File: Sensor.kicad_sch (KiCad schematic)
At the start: 28 parts, among them J27 *, SW2 *, U7 *, U8 *, U9 LSM6DSV

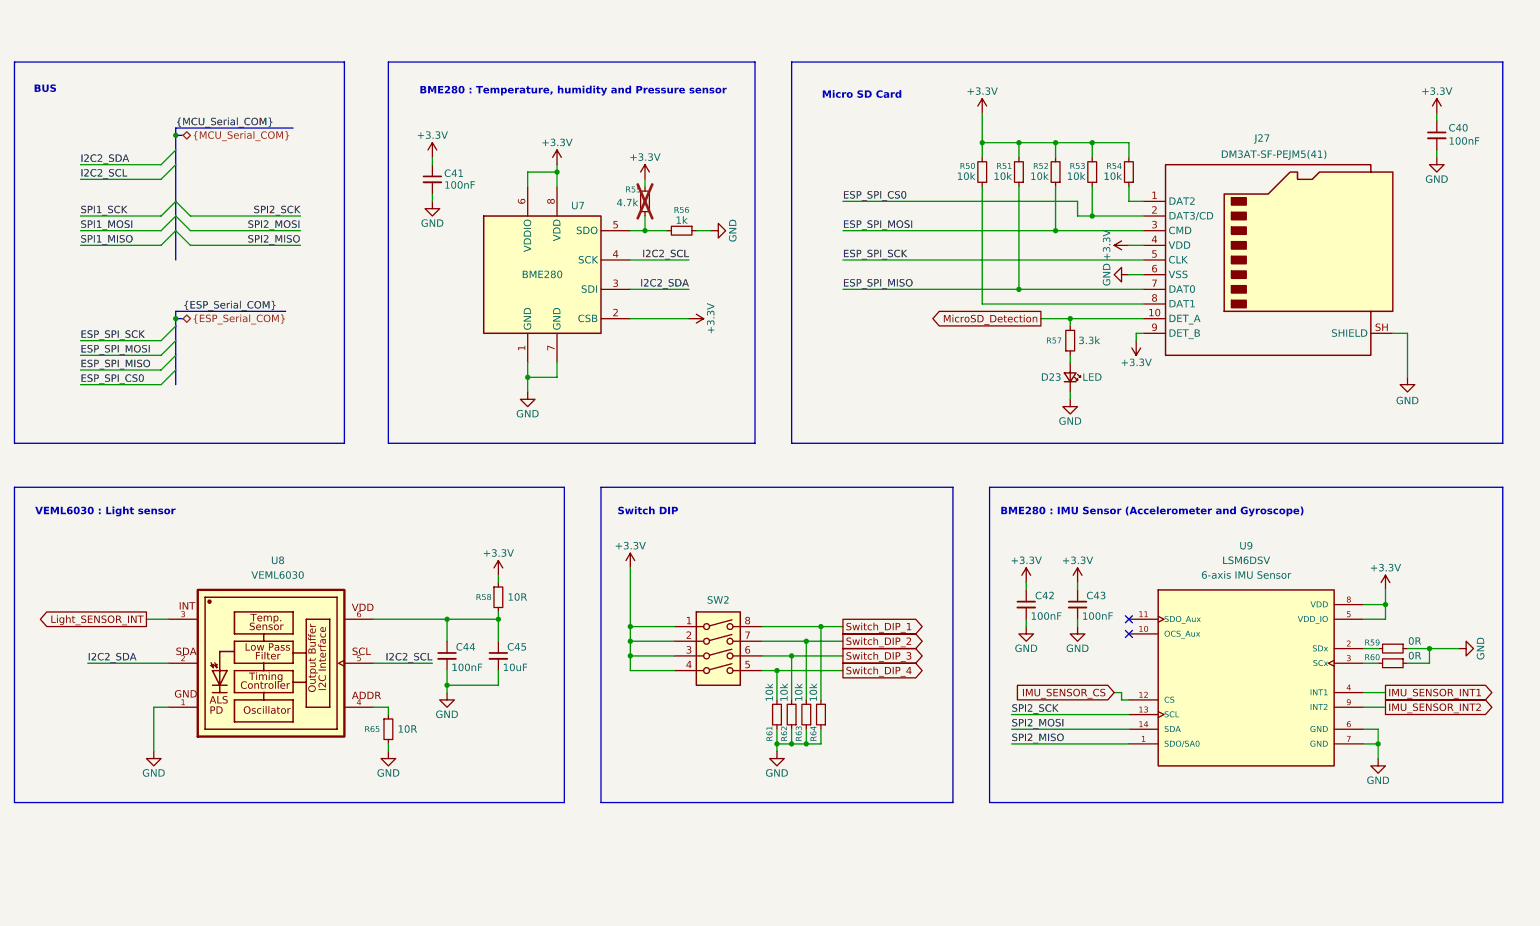
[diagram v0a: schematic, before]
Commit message: [Project][Added] CI/CD environment
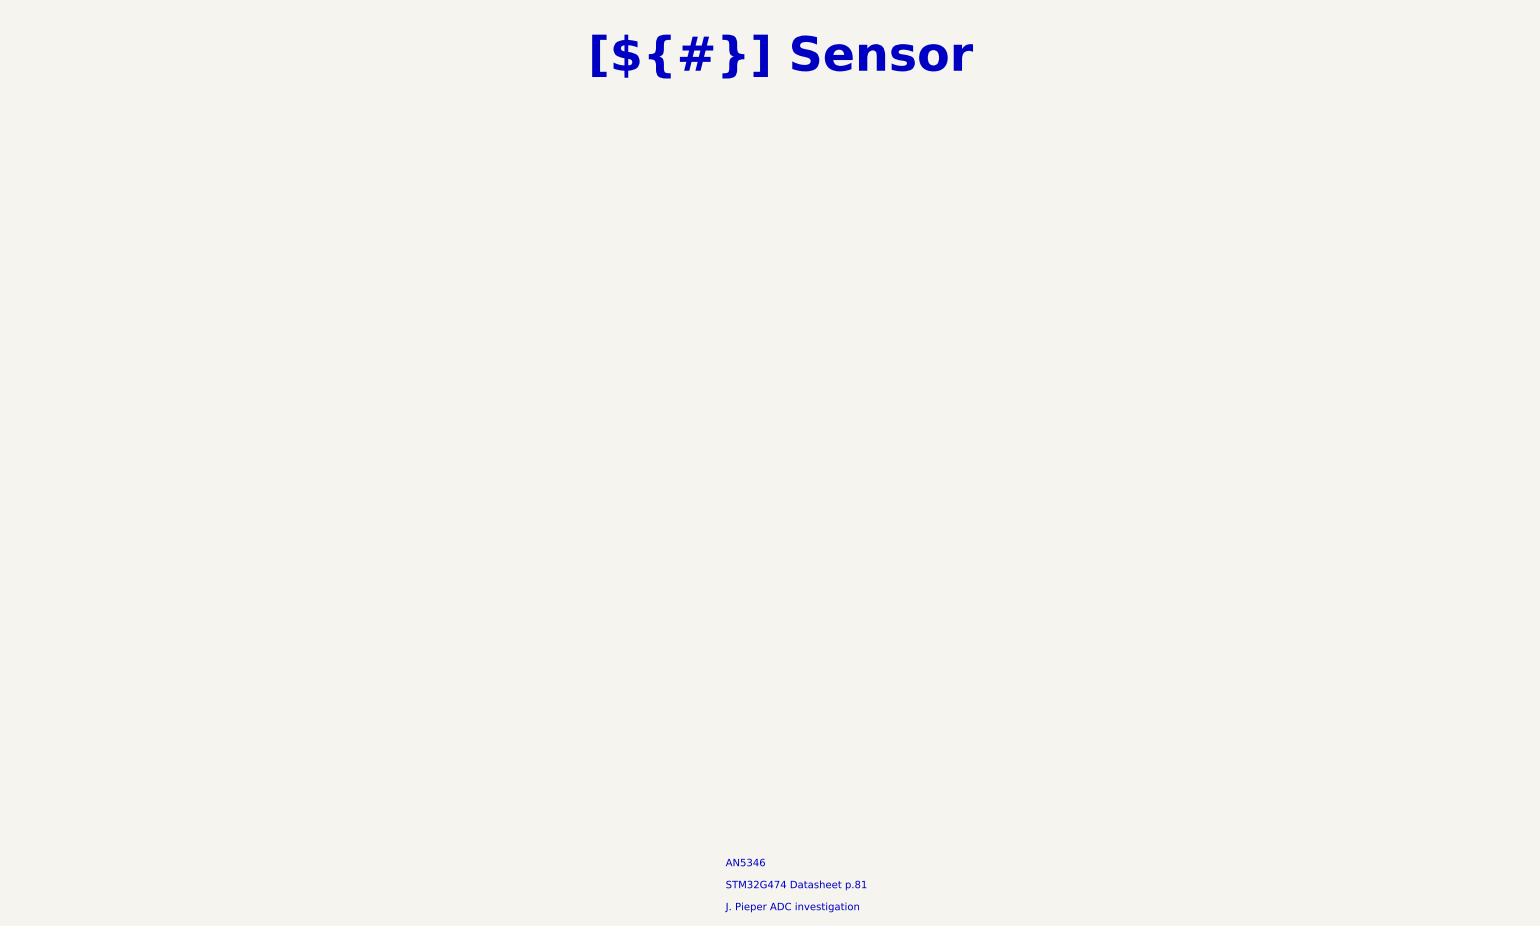
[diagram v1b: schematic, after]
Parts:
- removed C40, C41, C42, C43, C44: 100nF, Capacitor_SMD:C_0603_1608Metric_Pad1.08x0.95mm_HandSolder, symbol Device:C_Small
- removed C45: 10uF, Capacitor_SMD:C_0603_1608Metric_Pad1.08x0.95mm_HandSolder, symbol Device:C_Small
- removed D23: 5V, LED_SMD:LED_0805_2012Metric_Pad1.15x1.40mm_HandSolder, symbol Device:LED_Small
- removed J27: *, Connector_Card:microSD_HC_Hirose_DM3AT-SF-PEJM5, symbol Connector:Micro_SD_Card_Det2
- removed R50, R51, R52, R53, R54, R61, R62, R63, R64: 10k, Resistor_SMD:R_0603_1608Metric_Pad0.98x0.95mm_HandSolder, symbol Device:R_Small
- removed R55: 4.7k, Resistor_SMD:R_0603_1608Metric_Pad0.98x0.95mm_HandSolder, symbol Device:R_Small
- removed R56: 1k, Resistor_SMD:R_0603_1608Metric_Pad0.98x0.95mm_HandSolder, symbol Device:R_Small
- removed R57: 3.3k, Resistor_SMD:R_0603_1608Metric_Pad0.98x0.95mm_HandSolder, symbol Device:R_Small
- removed R58, R65: 10R, Resistor_SMD:R_0603_1608Metric_Pad0.98x0.95mm_HandSolder, symbol Device:R_Small
- removed R59, R60: 0R, Resistor_SMD:R_0603_1608Metric_Pad0.98x0.95mm_HandSolder, symbol Device:R_Small
- removed SW2: *, Button_Switch_SMD:SW_DIP_SPSTx04_Slide_Copal_CHS-04B_W7.62mm_P1.27mm, symbol Switch:SW_DIP_x04
- removed U7: *, Package_LGA:Bosch_LGA-8_2.5x2.5mm_P0.65mm_ClockwisePinNumbering, symbol Sensor:BME280
- removed U8: *, P_Specific_Footprint:VISHAY_VEML6030_2X2X0.87, symbol P_Sensor:VEML6030
- removed U9: LSM6DSV, P_LGA:LGA-14_3X2.5_P0.83mm, symbol P_Sensor:LSM6DSV
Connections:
- no-connect marks 2 -> 0
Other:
- note added: "AN5346"
- note added: "J. Pieper ADC investigation"
- note added: "STM32G474 Datasheet p.81"
- note removed: "BME280 : IMU Sensor (Accelerometer and Gyroscope)"
- note removed: "BME280 : Temperature, humidity and Pressure sensor"
- note removed: "BUS"
- note removed: "Micro SD Card"
- note removed: "Switch DIP"
- note removed: "VEML6030 : Light sensor"
- company: Nexvantis -> ${COMPANY}
- title: Data Acquisition Board -> Sensor

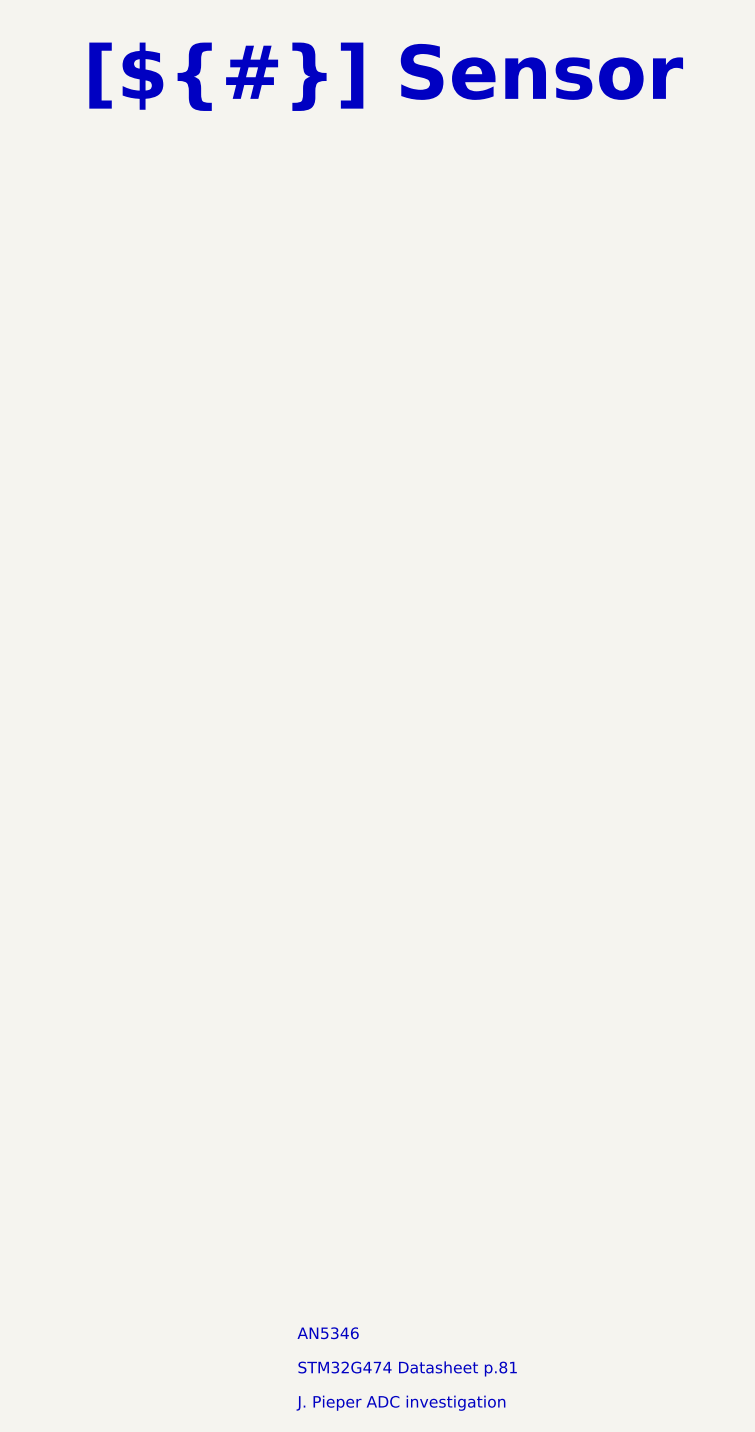
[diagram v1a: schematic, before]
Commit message: [Project][Added] CI/CD environment
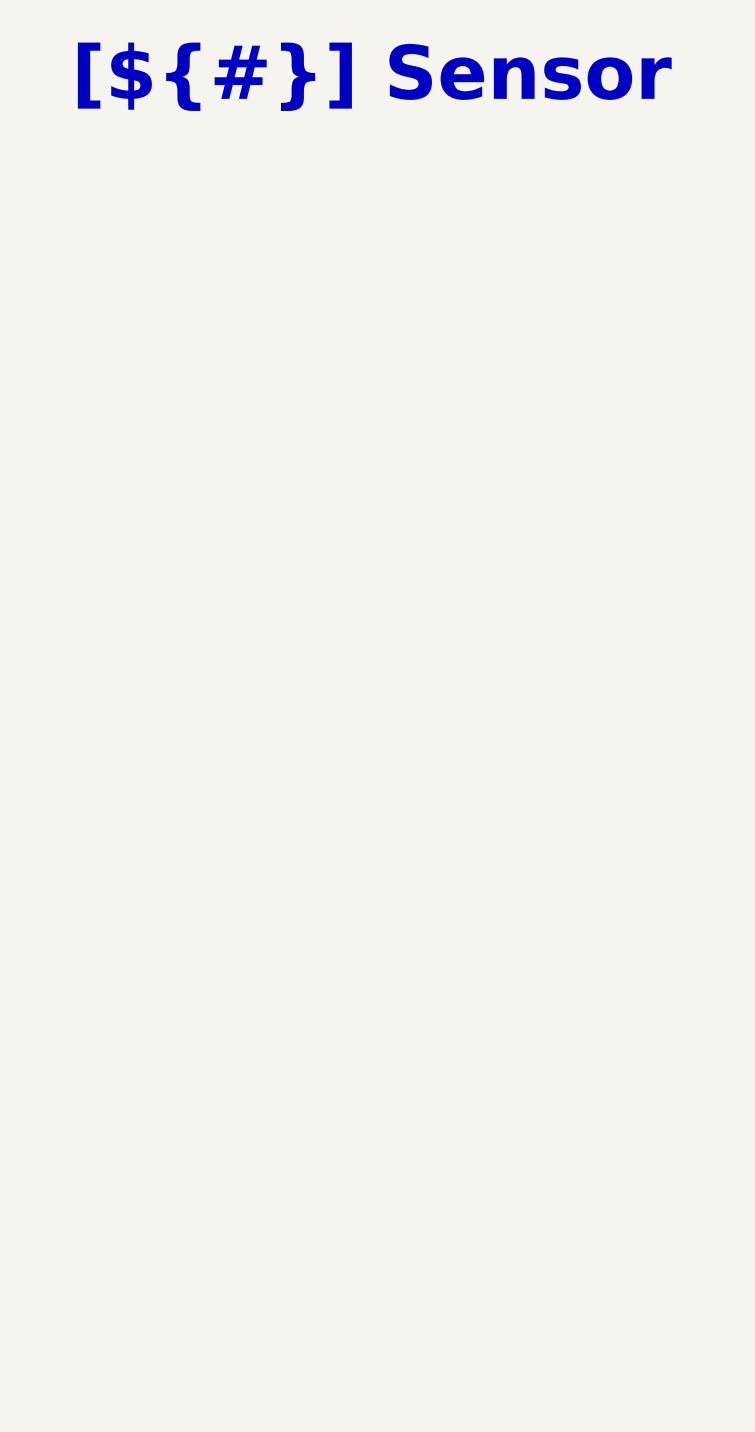
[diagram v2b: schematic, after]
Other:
- note removed: "AN5346"
- note removed: "J. Pieper ADC investigation"
- note removed: "STM32G474 Datasheet p.81"
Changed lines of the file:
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@@
 (kicad_sch
-	(version 20260306)
+	(version 20250114)
 	(generator "eeschema")
-	(generator_version "10.0")
+	(generator_version "9.0")
 	(paper "A4")
 	(title_block
@@
 		(company "${COMPANY}")
 	)
-	(text "J. Pieper ADC investigation"
-		(exclude_from_sim no)
-		(at 142.24 170.18 0)
-		(effects
-			(font
-				(face "Arial")
-				(size 1.27 1.27)
-				(color 0 0 0 1)
-			)
-			(justify left bottom)
-			(href "https://jpieper.com/2023/07/24/stm32g4-adc-performance-part-2/")
-		)
-	)
-	(text "STM32G474 Datasheet p.81"
-		(exclude_from_sim no)
-		(at 142.24 166.37 0)
-		(effects
-			(font
-				(face "Arial")
-				(size 1.27 1.27)
-				(color 0 0 0 1)
-			)
-			(justify left bottom)
-			(href "https://www.st.com/resource/en/datasheet/stm32g474cb.pdf")
-		)
-	)
-	(text "AN5346"
-		(exclude_from_sim no)
-		(at 142.24 162.56 0)
-		(effects
-			(font
-				(face "Arial")
-				(size 1.27 1.27)
-				(color 0 0 0 1)
-			)
-			(justify left bottom)
-			(href "https://www.st.com/resource/en/application_note/an5346-stm32g4-adc-use-tips-and-recommendations-stmicroelectronics.pdf")
-		)
-	)
 	(text_box "[${#}] ${TITLE}"
 		(exclude_from_sim no)
-		(at 115.57 15.24 0)
+		(at 114.3 15.24 0)
 		(size 72.39 12.7)
 		(margins 4.4999 4.4999 4.4999 4.4999)

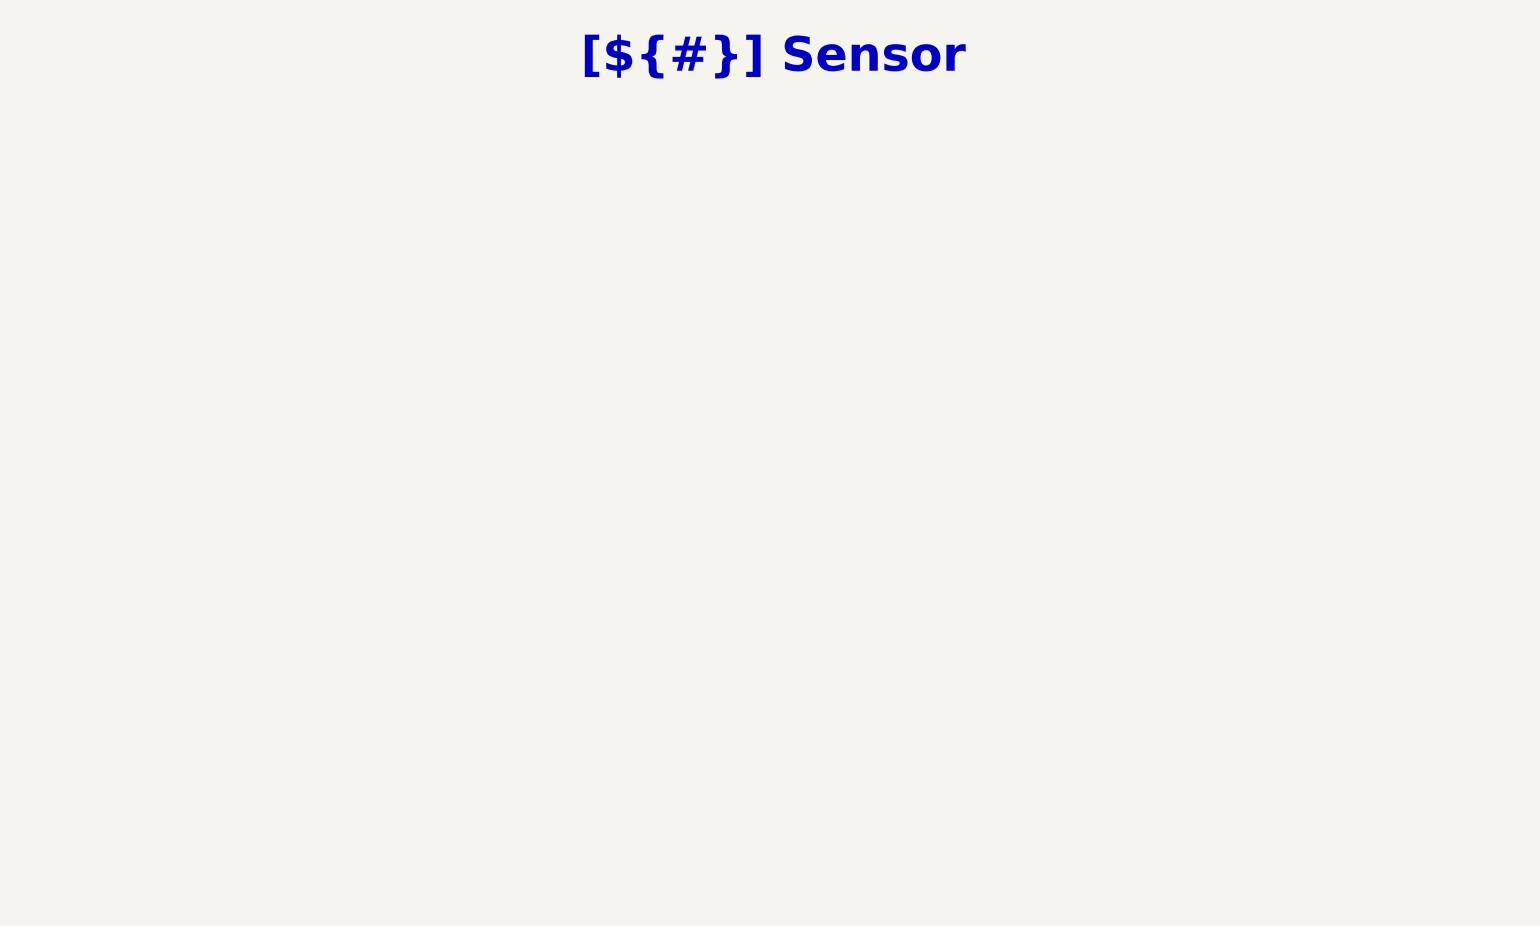
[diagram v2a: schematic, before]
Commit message: [Schematic][Add] Sensor, add schematic
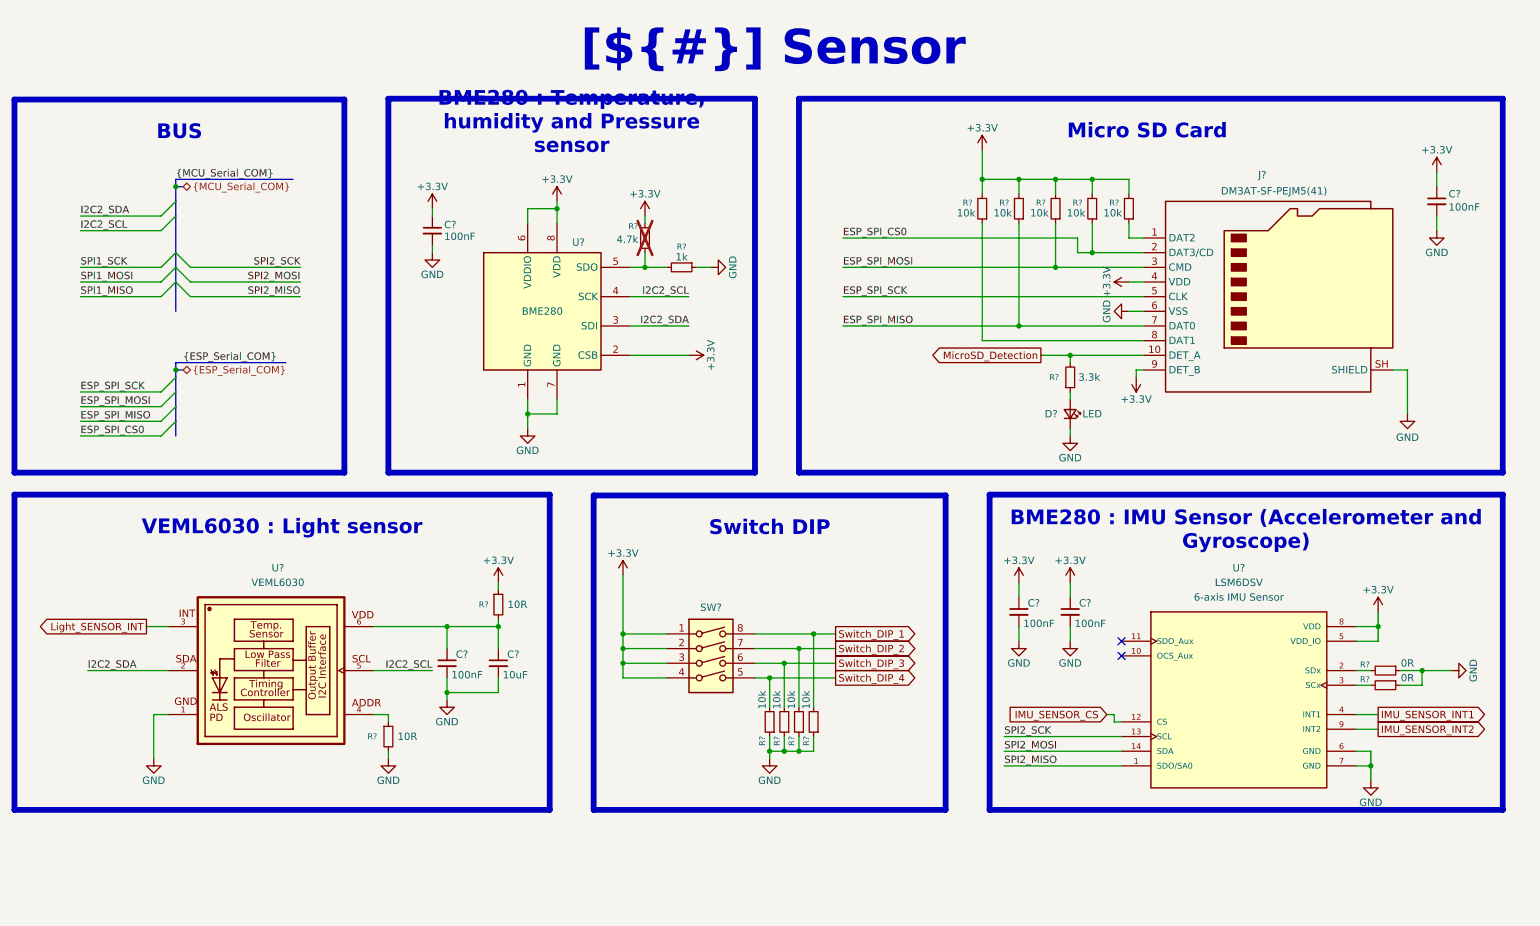
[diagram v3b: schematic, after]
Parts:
- added C? (x5): 100nF, Capacitor_SMD:C_0603_1608Metric_Pad1.08x0.95mm_HandSolder, symbol Device:C_Small
- added C?: 10uF, Capacitor_SMD:C_0603_1608Metric_Pad1.08x0.95mm_HandSolder, symbol Device:C_Small
- added D?: 5V, LED_SMD:LED_0805_2012Metric_Pad1.15x1.40mm_HandSolder, symbol Device:LED_Small
- added J?: *, Connector_Card:microSD_HC_Hirose_DM3AT-SF-PEJM5, symbol Connector:Micro_SD_Card_Det2
- added R? (x9): 10k, Resistor_SMD:R_0603_1608Metric_Pad0.98x0.95mm_HandSolder, symbol Device:R_Small
- added R?: 3.3k, Resistor_SMD:R_0603_1608Metric_Pad0.98x0.95mm_HandSolder, symbol Device:R_Small
- added R? (x2): 10R, Resistor_SMD:R_0603_1608Metric_Pad0.98x0.95mm_HandSolder, symbol Device:R_Small
- added R?: 1k, Resistor_SMD:R_0603_1608Metric_Pad0.98x0.95mm_HandSolder, symbol Device:R_Small
- added R? (x2): 0R, Resistor_SMD:R_0603_1608Metric_Pad0.98x0.95mm_HandSolder, symbol Device:R_Small
- added R?: 4.7k, Resistor_SMD:R_0603_1608Metric_Pad0.98x0.95mm_HandSolder, symbol Device:R_Small
- added SW?: *, Button_Switch_SMD:SW_DIP_SPSTx04_Slide_Copal_CHS-04B_W7.62mm_P1.27mm, symbol Switch:SW_DIP_x04
- added U?: *, Package_LGA:Bosch_LGA-8_2.5x2.5mm_P0.65mm_ClockwisePinNumbering, symbol Sensor:BME280
- added U?: *, P_Specific_Footprint:VISHAY_VEML6030_2X2X0.87, symbol P_Sensor:VEML6030
- added U?: LSM6DSV, P_LGA:LGA-14_3X2.5_P0.83mm, symbol P_Sensor:LSM6DSV
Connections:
- new net: C?.1, C?.1, R?.2, U?.6
- new net: D?.2 (A), R?.1
- new net: J?.1 (DAT2), R?.1
- new net: J?.8 (DAT1), R?.1
- new net: R?.1, U?.4
- new net: R?.1, R?.2, U?.5 (SDO)
- new net: R?.2, U?.2 (SDx)
- new net: R?.2, U?.3 (SCx)
- new net +3.3V: C?.1, C?.1, C?.1, C?.1, J?.4 (VDD), J?.9 (DET_B), R?.1, R?.2, R?.2, R?.2, R?.2, R?.2, R?.2, SW?.1, SW?.2, SW?.3, SW?.4, U?.2 (CSB), U?.5 (VDD_IO), U?.6 (VDDIO), U?.8 (VDD), U?.8 (VDD)
- new net ESP_SPI_CS0: J?.2 (DAT3/CD), R?.1
- new net ESP_SPI_MISO: J?.7 (DAT0), R?.1
- new net ESP_SPI_MOSI: J?.3 (CMD), R?.1
- new net ESP_SPI_SCK: J?.5 (CLK)
- new net GND: C?.2, C?.2, C?.2, C?.2, C?.2, C?.2, D?.1 (K), J?.6 (VSS), J?.SH (SHIELD), R?.1, R?.1, R?.1, R?.1, R?.1, R?.1, R?.1, R?.2, U?.1, U?.1 (GND), U?.6 (GND), U?.7 (GND), U?.7 (GND)
- new net I2C2_SCL: U?.4 (SCK), U?.5
- new net I2C2_SDA: U?.2, U?.3 (SDI)
- new net IMU_SENSOR_CS: U?.12 (CS)
- new net IMU_SENSOR_INT1: U?.4 (INT1)
- new net IMU_SENSOR_INT2: U?.9 (INT2)
- new net Light_SENSOR_INT: U?.3
- new net MicroSD_Detection: J?.10 (DET_A), R?.2
- new net SPI2_MISO: U?.1 (SDO/SA0)
- new net SPI2_MOSI: U?.14 (SDA)
- new net SPI2_SCK: U?.13 (SCL)
- new net Switch_DIP_1: R?.2, SW?.8
- new net Switch_DIP_2: R?.2, SW?.7
- new net Switch_DIP_3: R?.2, SW?.6
- new net Switch_DIP_4: R?.2, SW?.5
- no-connect marks 0 -> 2

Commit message: [Schematic][Modify] Annotation of all  the components
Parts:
- gave numbers to parts that had none: 28

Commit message: [Schematic][Modify] Annotation of all  the components
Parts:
- renumbered C56 to C51, C51 to C52, C54 to C53, C55 to C54, C52 to C55, C53 to C56, R72 to R64, R73 to R65, R74 to R66, R76 to R67, R77 to R68, R66 to R69, R67 to R70, R75 to R71, R65 to R72, R78 to R73, R79 to R74, R68 to R75, R69 to R76, R70 to R77, R71 to R78, R64 to R79, U9 to U10, U10 to U9
